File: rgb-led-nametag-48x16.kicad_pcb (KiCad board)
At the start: 4 copper layers, 84 x 28.8 mm, 130 parts, among them J1 USB_C_Receptacle_USB2.0, J2 TagConnect_TC2030_SWD, Q1 CJ3139K, Q10 CJ3139K, Q11 CJ3139K, Q12 CJ3139K, Q13 CJ3139K, Q14 CJ3139K, Q15 CJ3139K, Q16 CJ3139K, Q2 CJ3139K, Q3 CJ3139K, Q4 CJ3139K, Q5 CJ3139K, Q6 CJ3139K, Q7 CJ3139K, Q8 CJ3139K, Q9 CJ3139K, U1 led-panel-16x16, U10 74HC595, U11 74HC595, U12 74HC595, U13 74HC595, U14 74HC595, U15 74HC595, U16 led-panel-16x16, U17 74HC595, U18 74HC595, U19 74HC595, U2 74HC595, U20 74HC595, U21 74HC595, U22 74HC595, U23 74HC595, U24 ESP32-PICO-D4, U25 STM32F722RETx, U26 SRV05-4, U27 TPS63001, U3 74HC595, U4 74HC595, U5 74HC595, U6 74HC595, U7 74HC595, U8 74HC595, U9 led-panel-16x16

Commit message: Add preliminary ESP32 power layout
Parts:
- added C40: 100nF, Capacitor_SMD:C_0402_1005Metric, F.Cu at (165.9, 109.0)
- added R6: 100k, Resistor_SMD:R_0402_1005Metric, F.Cu at (167.0, 109.0)
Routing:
- net /Sheet620161B9/3V3: track 15.1 -> 39.1 mm, vias 6 -> 7
- net Net-(C25-Pad2): track 0.00 -> 6.49 mm
- net Net-(AE1-Pad1): track 0.00 -> 3.86 mm
- net /Sheet620161B9/EN: track 0.00 -> 2.75 mm
- net GND: track 62.0 -> 62.7 mm, vias 39 -> 40
- net /Sheet620161B9/~CS: track 54.9 -> 54.3 mm
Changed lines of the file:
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@@
     (thickness 1.6)
     (drawings 8)
-    (tracks 2976)
+    (tracks 3005)
     (zones 0)
-    (modules 130)
+    (modules 132)
     (nets 468)
   )
@@
   )
   (setup
-    (last_trace_width 0.127)
+    (last_trace_width 0.5)
     (user_trace_width 0.25)
     (user_trace_width 0.5)
@@
     (add_net VBUS)
   )
+  (module Resistor_SMD:R_0402_1005Metric (layer F.Cu)
+    (at 166.975 109 270)
+    (descr "Resistor SMD 0402 (1005 Metric), square (rectangular) end terminal, IPC_7351 nominal, (Body size source: IPC-SM-782 page 72, https://www.pcb-3d.com/wordpress/wp-content/uploads/ipc-sm-782a_amendment_1_and_2.pdf), generated with kicad-footprint-generator")
+    (tags resistor)
+    (attr smd)
+    (fp_text reference R6 (at 0 -1.17 90) (layer F.SilkS)
+      (effects (font (size 1 1) (thickness 0.15)))
+    )
+    (fp_text value 100k (at 0 1.17 90) (layer F.Fab)
+      (effects (font (size 1 1) (thickness 0.15)))
+    )
+    (fp_text user %R (at 0 0 90) (layer F.Fab)
+      (effects (font (size 0.26 0.26) (thickness 0.04)))
+    )
+    (fp_line (start -0.525 0.27) (end -0.525 -0.27) (layer F.Fab) (width 0.1))
+    (fp_line (start -0.525 -0.27) (end 0.525 -0.27) (layer F.Fab) (width 0.1))
+    (fp_line (start 0.525 -0.27) (end 0.525 0.27) (layer F.Fab) (width 0.1))
+    (fp_line (start 0.525 0.27) (end -0.525 0.27) (layer F.Fab) (width 0.1))
+    (fp_line (start -0.153641 -0.38) (end 0.153641 -0.38) (layer F.SilkS) (width 0.12))
+    (fp_line (start -0.153641 0.38) (end 0.153641 0.38) (layer F.SilkS) (width 0.12))
+    (fp_line (start -0.93 0.47) (end -0.93 -0.47) (layer F.CrtYd) (width 0.05))
+    (fp_line (start -0.93 -0.47) (end 0.93 -0.47) (layer F.CrtYd) (width 0.05))
+    (fp_line (start 0.93 -0.47) (end 0.93 0.47) (layer F.CrtYd) (width 0.05))
+    (fp_line (start 0.93 0.47) (end -0.93 0.47) (layer F.CrtYd) (width 0.05))
+    (pad 2 smd roundrect (at 0.51 0 270) (size 0.54 0.64) (layers F.Cu F.Paste F.Mask) (roundrect_rratio 0.25)
+      (net 376 /Sheet620161B9/3V3))
+    (pad 1 smd roundrect (at -0.51 0 270) (size 0.54 0.64) (layers F.Cu F.Paste F.Mask) (roundrect_rratio 0.25)
+      (net 381 /Sheet620161B9/EN))
+    (model ${KISYS3DMOD}/Resistor_SMD.3dshapes/R_0402_1005Metric.wrl
+      (at (xyz 0 0 0))
+      (scale (xyz 1 1 1))
+      (rotate (xyz 0 0 0))
+    )
+  )
+  (module Capacitor_SMD:C_0402_1005Metric (layer F.Cu)
+    (at 165.95 109 90)
+    (descr "Capacitor SMD 0402 (1005 Metric), square (rectangular) end terminal, IPC_7351 nominal, (Body size source: IPC-SM-782 page 76, https://www.pcb-3d.com/wordpress/wp-content/uploads/ipc-sm-782a_amendment_1_and_2.pdf), generated with kicad-footprint-generator")
+    (tags capacitor)
+    (attr smd)
+    (fp_text reference C40 (at 0 -1.16 90) (layer F.SilkS)
+      (effects (font (size 1 1) (thickness 0.15)))
+    )
+    (fp_text value 100nF (at 0 1.16 90) (layer F.Fab)
+      (effects (font (size 1 1) (thickness 0.15)))
+    )
+    (fp_text user %R (at 0 0 90) (layer F.Fab)
+      (effects (font (size 0.25 0.25) (thickness 0.04)))
+    )
+    (fp_line (start -0.5 0.25) (end -0.5 -0.25) (layer F.Fab) (width 0.1))
+    (fp_line (start -0.5 -0.25) (end 0.5 -0.25) (layer F.Fab) (width 0.1))
+    (fp_line (start 0.5 -0.25) (end 0.5 0.25) (layer F.Fab) (width 0.1))
+    (fp_line (start 0.5 0.25) (end -0.5 0.25) (layer F.Fab) (width 0.1))
+    (fp_line (start -0.107836 -0.36) (end 0.107836 -0.36) (layer F.SilkS) (width 0.12))
+    (fp_line (start -0.107836 0.36) (end 0.107836 0.36) (layer F.SilkS) (width 0.12))
+    (fp_line (start -0.91 0.46) (end -0.91 -0.46) (layer F.CrtYd) (width 0.05))
+    (fp_line (start -0.91 -0.46) (end 0.91 -0.46) (layer F.CrtYd) (width 0.05))
+    (fp_line (start 0.91 -0.46) (end 0.91 0.46) (layer F.CrtYd) (width 0.05))
+    (fp_line (start 0.91 0.46) (end -0.91 0.46) (layer F.CrtYd) (width 0.05))
+    (pad 2 smd roundrect (at 0.48 0 90) (size 0.56 0.62) (layers F.Cu F.Paste F.Mask) (roundrect_rratio 0.25)
+      (net 2 GND))
+    (pad 1 smd roundrect (at -0.48 0 90) (size 0.56 0.62) (layers F.Cu F.Paste F.Mask) (roundrect_rratio 0.25)
+      (net 381 /Sheet620161B9/EN))
+    (model ${KISYS3DMOD}/Capacitor_SMD.3dshapes/C_0402_1005Metric.wrl
+      (at (xyz 0 0 0))
+      (scale (xyz 1 1 1))
+      (rotate (xyz 0 0 0))
+    )
+  )
   (module Capacitor_SMD:C_0402_1005Metric (layer F.Cu)
     (at 161.575 115.825 90)
@@
   (via (at 161.575 117) (size 0.45) (drill 0.2) (layers F.Cu B.Cu) (net 2))
   (segment (start 161.575 116.305) (end 161.575 117) (width 0.127) (layer F.Cu) (net 2))
+  (via (at 165.95 107.875) (size 0.45) (drill 0.2) (layers F.Cu B.Cu) (net 2))
+  (segment (start 165.95 108.52) (end 165.95 107.875) (width 0.127) (layer F.Cu) (net 2))
   (via (at 156.3 120.5) (size 0.45) (drill 0.2) (layers F.Cu B.Cu) (net 3))
   (segment (start 148.9 120.5) (end 156.3 120.5) (width 0.127) (layer In2.Cu) (net 3))
@@
   (segment (start 153.13 111.584942) (end 154.08 110.634942) (width 0.127) (layer F.Cu) (net 346))
   (segment (start 153.13 112.59) (end 153.13 111.584942) (width 0.127) (layer F.Cu) (net 346))
+  (segment (start 169.289411 117.414411) (end 172 120.125) (width 0.5) (layer F.Cu) (net 375))
+  (segment (start 172 120.125) (end 172.025 120.125) (width 0.5) (layer F.Cu) (net 375))
   (segment (start 161.05 107.275) (end 161.05 106.15) (width 0.127) (layer F.Cu) (net 376))
   (segment (start 164.75 112.475) (end 165.925 112.475) (width 0.127) (layer F.Cu) (net 376))
@@
   (segment (start 161.67 115.345) (end 162.3 115.975) (width 0.127) (layer F.Cu) (net 376))
   (segment (start 161.575 115.345) (end 161.67 115.345) (width 0.127) (layer F.Cu) (net 376))
+  (segment (start 166.975 110.1) (end 166.5 110.575) (width 0.127) (layer F.Cu) (net 376))
+  (segment (start 166.975 109.51) (end 166.975 110.1) (width 0.127) (layer F.Cu) (net 376))
+  (via (at 160.475 106.1) (size 0.45) (drill 0.2) (layers F.Cu B.Cu) (net 376))
+  (segment (start 160.48 106.105) (end 160.475 106.1) (width 0.127) (layer F.Cu) (net 376))
+  (segment (start 161.05 106.105) (end 160.48 106.105) (width 0.127) (layer F.Cu) (net 376))
+  (segment (start 160.475 106.1) (end 162.85 106.1) (width 0.5) (layer In2.Cu) (net 376))
+  (segment (start 165.925 109.175) (end 165.925 110.775) (width 0.5) (layer In2.Cu) (net 376))
+  (segment (start 162.85 106.1) (end 165.925 109.175) (width 0.5) (layer In2.Cu) (net 376))
+  (segment (start 166.125 110.575) (end 165.925 110.775) (width 0.5) (layer In2.Cu) (net 376))
+  (segment (start 166.5 110.575) (end 166.125 110.575) (width 0.5) (layer In2.Cu) (net 376))
+  (segment (start 165.925 113.175) (end 165.025 114.075) (width 0.5) (layer In2.Cu) (net 376))
+  (segment (start 165.925 110.775) (end 165.925 113.175) (width 0.5) (layer In2.Cu) (net 376))
+  (segment (start 157.925 114.1) (end 160.1 114.1) (width 0.5) (layer In2.Cu) (net 376))
+  (segment (start 164.800001 113.850001) (end 165.025 114.075) (width 0.5) (layer In2.Cu) (net 376))
+  (segment (start 160.1 114.1) (end 160.349999 113.850001) (width 0.5) (layer In2.Cu) (net 376))
+  (segment (start 162.3 113.875002) (end 162.274999 113.850001) (width 0.5) (layer In2.Cu) (net 376))
+  (segment (start 162.3 115.975) (end 162.3 113.875002) (width 0.5) (layer In2.Cu) (net 376))
+  (segment (start 162.274999 113.850001) (end 164.800001 113.850001) (width 0.5) (layer In2.Cu) (net 376))
+  (segment (start 160.349999 113.850001) (end 162.274999 113.850001) (width 0.5) (layer In2.Cu) (net 376))
+  (segment (start 164.75 112.975) (end 166.675 112.975) (width 0.25) (layer F.Cu) (net 377))
+  (segment (start 167.075 113.375) (end 166.675 112.975) (width 0.5) (layer F.Cu) (net 377))
+  (segment (start 167.075 115.2) (end 167.075 113.375) (width 0.5) (layer F.Cu) (net 377))
+  (segment (start 168.610589 116.735589) (end 167.075 115.2) (width 0.5) (layer F.Cu) (net 377))
   (segment (start 160.55 114.175) (end 160.55 115.85) (width 0.127) (layer F.Cu) (net 378))
   (segment (start 160.55 115.85) (end 159.525 116.875) (width 0.127) (layer F.Cu) (net 378))
@@
   (segment (start 130.6 122.425) (end 130.45 122.275) (width 0.127) (layer F.Cu) (net 379))
   (segment (start 130.45 122.275) (end 108.7 122.275) (width 0.127) (layer F.Cu) (net 379))
+  (segment (start 165.95 109.48) (end 165.95 109.475) (width 0.127) (layer F.Cu) (net 381))
+  (segment (start 165.95 109.475) (end 166.975 108.45) (width 0.127) (layer F.Cu) (net 381))
+  (segment (start 164.75 109.475) (end 166.05 109.475) (width 0.127) (layer F.Cu) (net 381))
   (segment (start 111.557501 116.018161) (end 111.568161 116.018161) (width 0.127) (layer F.Cu) (net 382))
   (segment (start 111.568161 116.018161) (end 112.775 117.225) (width 0.127) (layer F.Cu) (net 382))
@@
   (segment (start 151.825 119) (end 151.825 119.275) (width 0.127) (layer F.Cu) (net 467))
   (segment (start 151.825 118.675) (end 151.825 119) (width 0.127) (layer F.Cu) (net 467))
-  (segment (start 151.825 119) (end 151.825 119.525) (width 0.127) (layer F.Cu) (net 467))
   (segment (start 151.825 119.275) (end 151.575 119.525) (width 0.127) (layer F.Cu) (net 467))
   (segment (start 151.575 119.525) (end 148.425 119.525) (width 0.127) (layer F.Cu) (net 467))

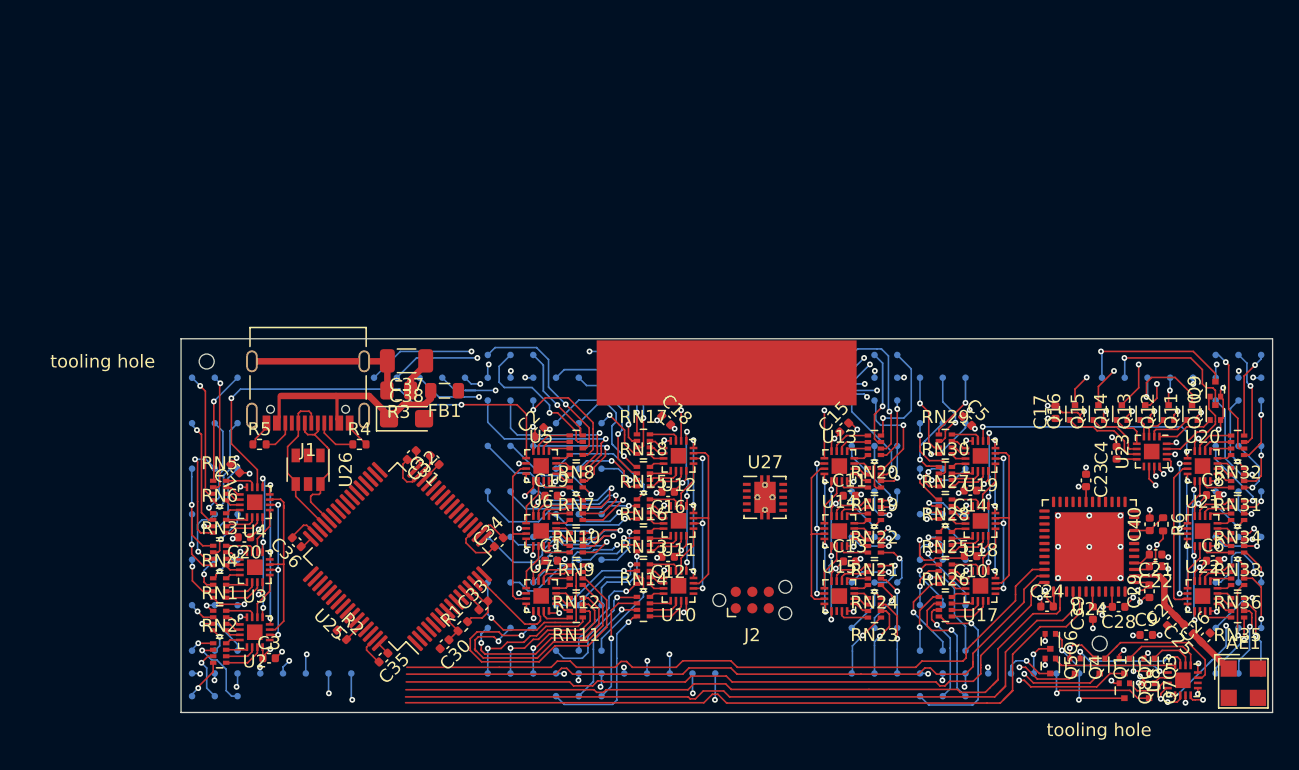
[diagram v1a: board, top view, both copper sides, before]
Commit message: Layout horizontal busses
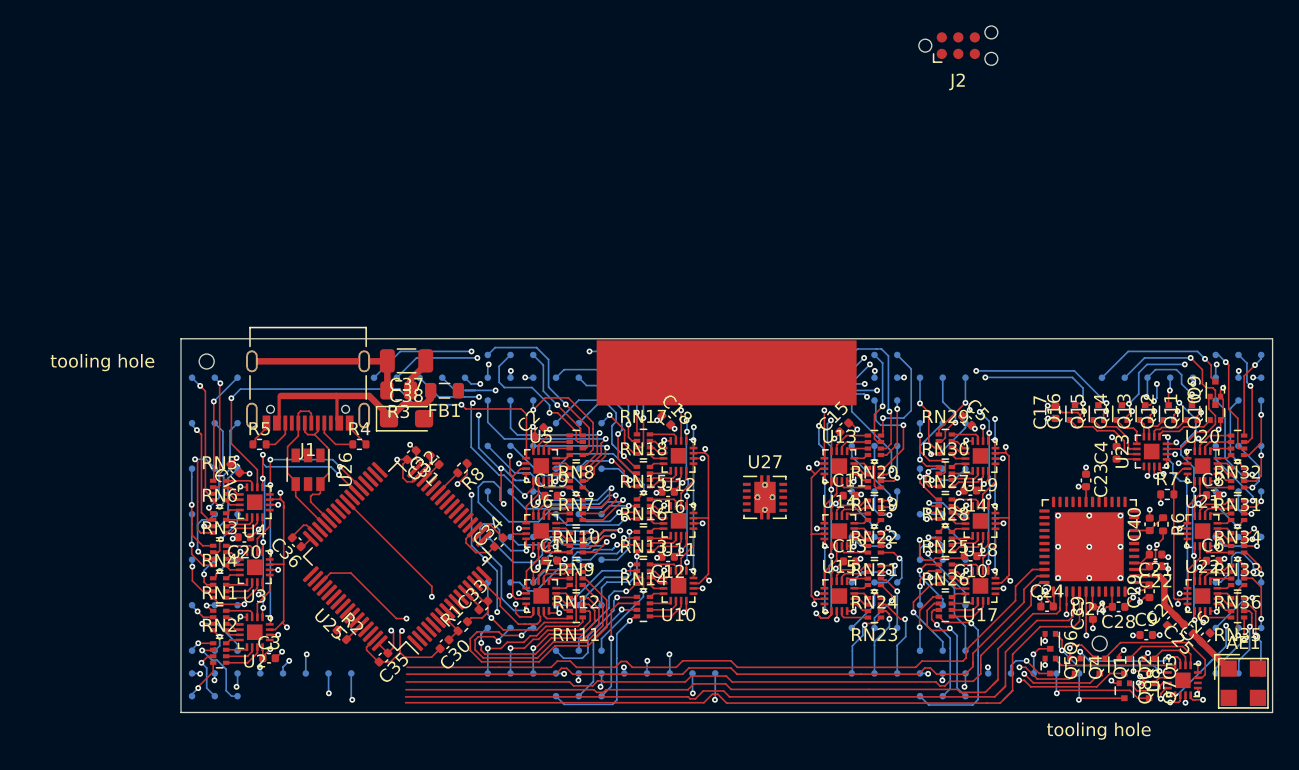
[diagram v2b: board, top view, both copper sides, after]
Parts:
- added R7: 470R, Resistor_SMD:R_0402_1005Metric, F.Cu at (167.3, 106.7)
- added R8: 33R, Resistor_SMD:R_0402_1005Metric, F.Cu at (113.1, 104.7)
- moved J2 45.5 mm to (151.2, 72.2)
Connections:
- net Net-(U24-Pad39) renamed /Sheet620161B9/SCL
- net Net-(U24-Pad42) renamed /Sheet620161B9/SDA
- U10 pad 10: /COL_~RST -> VBUS
- U11 pad 10: /COL_~RST -> VBUS
- U12 pad 10: /COL_~RST -> VBUS
- U13 pad 10: /COL_~RST -> VBUS
- U14 pad 10: /COL_~RST -> VBUS
- U15 pad 10: /COL_~RST -> VBUS
- U15 pad 14: /QSPI_D1 -> /QSPI_D0
- U17 pad 10: /COL_~RST -> VBUS
- U18 pad 10: /COL_~RST -> VBUS
- U19 pad 10: /COL_~RST -> VBUS
- U2 pad 10: /COL_~RST -> VBUS
- U20 pad 10: /COL_~RST -> VBUS
- U21 pad 10: /COL_~RST -> VBUS
- U22 pad 10: /COL_~RST -> VBUS
- U22 pad 14: /QSPI_D0 -> /QSPI_D1
- U23 pad 10: /ROW_~RST -> VBUS
- U23 pad 13: /ROW_~OE -> GND
- U25 pad 27: /QSPI_CLK -> Net-(R8-Pad2)
- U3 pad 10: /COL_~RST -> VBUS
- U4 pad 10: /COL_~RST -> VBUS
- U5 pad 10: /COL_~RST -> VBUS
- U6 pad 10: /COL_~RST -> VBUS
- U7 pad 10: /COL_~RST -> VBUS
- U8 pad 10: /ROW_~RST -> VBUS
- U8 pad 13: /ROW_~OE -> GND
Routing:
- net /COL_~OE: track 73.5 -> 201.7 mm, vias 18 -> 28
- net /COL_LATCH: track 71.1 -> 189.6 mm, vias 18 -> 27
- net /QSPI_CLK: track 76.6 -> 171.9 mm, vias 0 -> 12
- net /QSPI_D1: track 0.00 -> 73.6 mm, vias 0 -> 2
- net /COL_~RST: track 70.9 -> 0.00 mm, vias 18 -> 0
- net /Sheet620161B9/SDA: track 0.00 -> 57.9 mm, vias 0 -> 1
- net /Sheet620161B9/SCL: track 0.00 -> 55.9 mm, vias 0 -> 1
- net /QSPI_D0: track 0.00 -> 43.9 mm, vias 0 -> 2
- net /ROW_~OE: track 22.8 -> 0.00 mm, vias 2 -> 0
- net /ROW_~RST: track 22.5 -> 0.00 mm, vias 2 -> 0
- net VBUS: track 44.2 -> 56.9 mm, vias 56 -> 76
- net /Panel 2/sheet61A6C351/SIN: track 6.07 -> 17.1 mm
- net GND: track 62.7 -> 72.3 mm, vias 40 -> 45
- net /A15: track 60.7 -> 69.2 mm, vias 4 -> 5
- net /A9: track 81.2 -> 88.3 mm
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
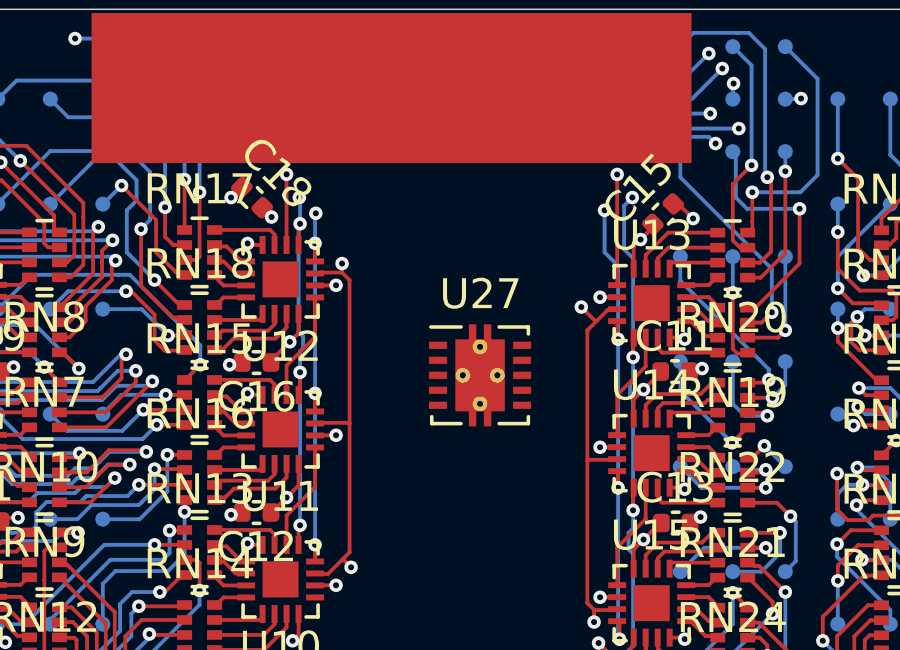
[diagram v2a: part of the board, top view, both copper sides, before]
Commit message: Layout 3V3 buck/boost converter
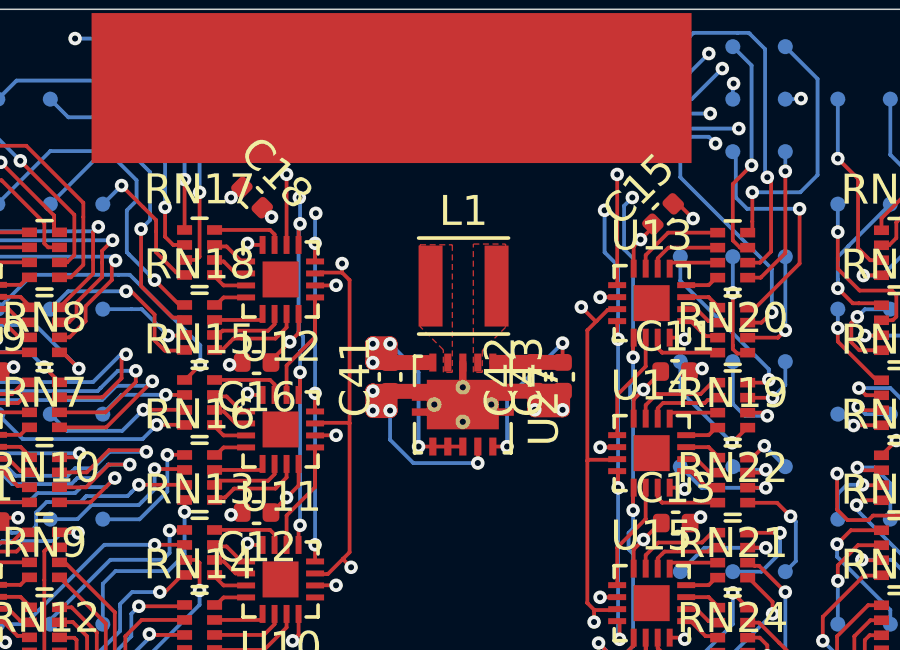
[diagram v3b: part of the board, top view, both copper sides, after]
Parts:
- added C41: 10uF, Capacitor_SMD:C_0402_1005Metric, F.Cu at (133.3, 107.0)
- added C42: 10uF, Capacitor_SMD:C_0402_1005Metric, F.Cu at (138.2, 107.0)
- added C43: 10uF, Capacitor_SMD:C_0402_1005Metric, F.Cu at (139.1, 107.0)
- added L1: 2.2uH, Inductor_SMD:L_Taiyo-Yuden_MD-3030, F.Cu at (135.8, 104.0)
- moved U27 1.13 mm to (135.8, 107.9), turned to 270 degrees
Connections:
- U27 pad 1: Net-(U27-Pad1) -> Net-(C42-Pad2)
- U27 pad 10: Net-(U27-Pad10) -> Net-(C42-Pad2)
- U27 pad 11: Net-(U27-Pad11) -> GND
- U27 pad 2: Net-(U27-Pad2) -> /L2
- U27 pad 3: Net-(U27-Pad11) -> GND
- U27 pad 4: Net-(U27-Pad4) -> /L1
- U27 pad 5: Net-(U27-Pad5) -> Net-(C41-Pad2)
- U27 pad 6: Net-(U27-Pad6) -> Net-(C41-Pad2)
- U27 pad 7: Net-(U27-Pad7) -> Net-(C41-Pad2)
- U27 pad 8: Net-(U27-Pad8) -> Net-(C41-Pad2)
- U27 pad 9: Net-(U27-Pad9) -> GND
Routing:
- net GND: track 72.3 -> 89.7 mm, vias 45 -> 51
- net Net-(C41-Pad2): track 0.00 -> 10.4 mm, vias 0 -> 4
- net Net-(C42-Pad2): track 0.00 -> 9.84 mm, vias 0 -> 2
- added copper zone on F.Cu, net /L1
- added copper zone on F.Cu, net /L2
